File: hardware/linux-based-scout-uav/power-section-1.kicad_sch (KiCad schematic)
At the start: 16 parts, among them J5 GSB1C41110SSHR, Q1 DMP3013SFV, Q2 DMP3013SFV, U11 TPS65217CRSLR, U9 CYPD3177-24LQ

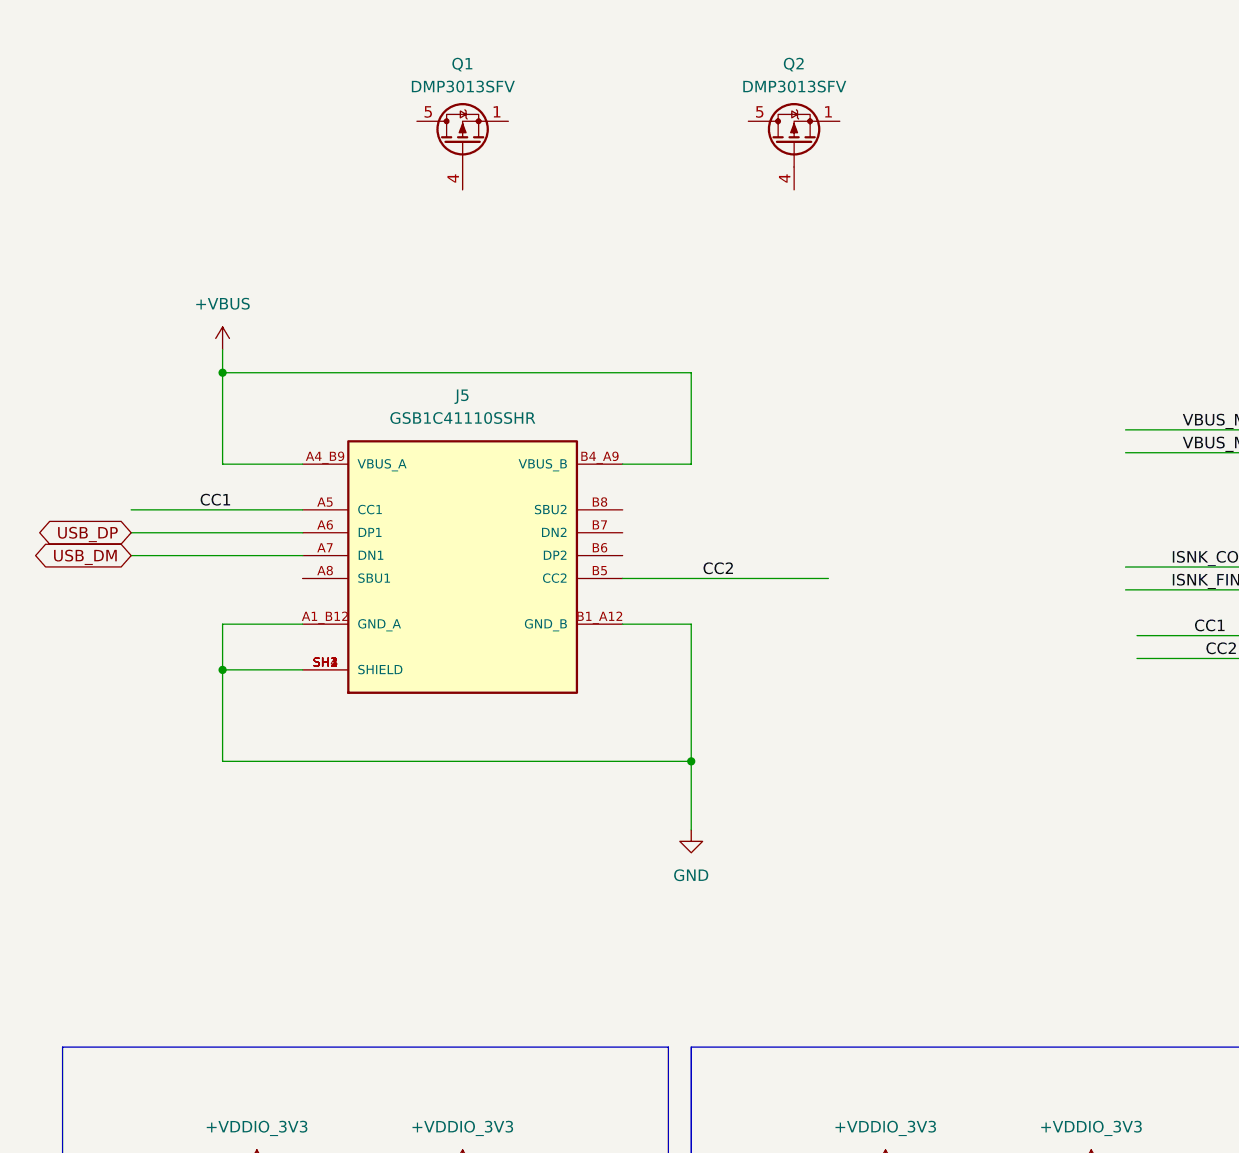
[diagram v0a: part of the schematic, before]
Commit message: Updated project to KiCad 9.0
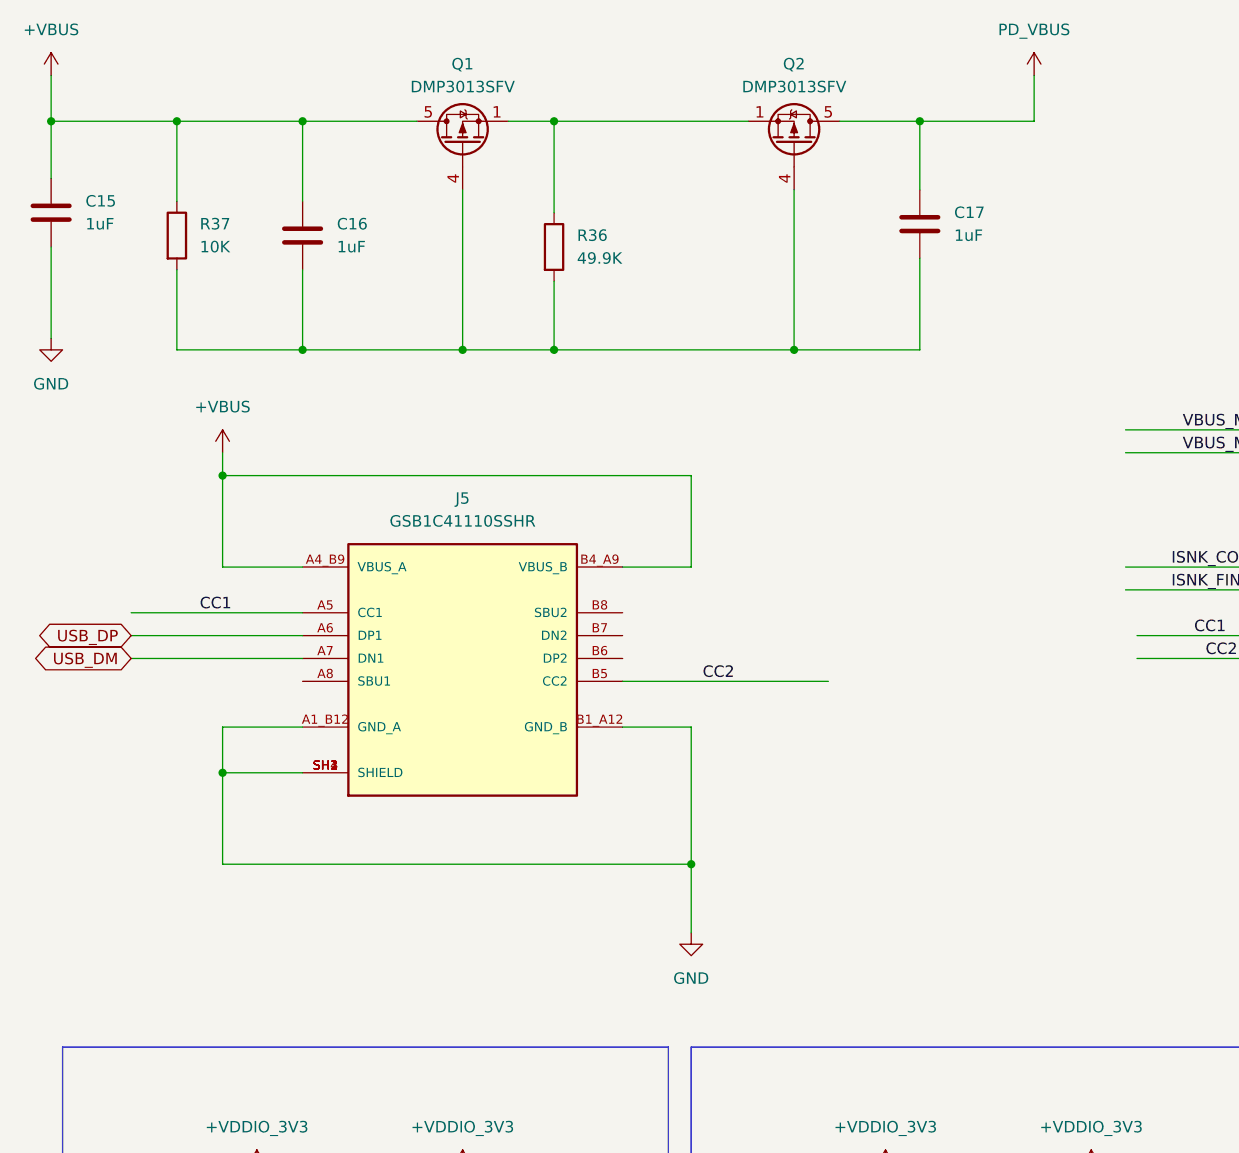
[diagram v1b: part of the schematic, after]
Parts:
- added C15, C16, C17: 1uF, symbol Device:C
- added R36: 49.9K, Resistor_SMD:R_0402_1005Metric, symbol Device:R
- added R37: 10K, Resistor_SMD:R_0402_1005Metric, symbol Device:R
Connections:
- net +VBUS: now also Q1.5 (D), C15.1, C16.1, R37.1
- net GND: now also C15.2
- net at Q1.1 (S), Q1.2 (S), Q1.3 (S): now also Q2.1 (S), Q2.2 (S), Q2.3 (S), R36.1
- net at Q1.4 (G): now also Q2.4 (G), C16.2, C17.2, R36.2, R37.2
- net PD_VBUS: now reaches Q2.5 (D)
- net PD_VBUS: now also C17.1
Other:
- moved on the sheet: J5, Q2
